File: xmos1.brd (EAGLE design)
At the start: 108 x 69.8 mm, 3 parts

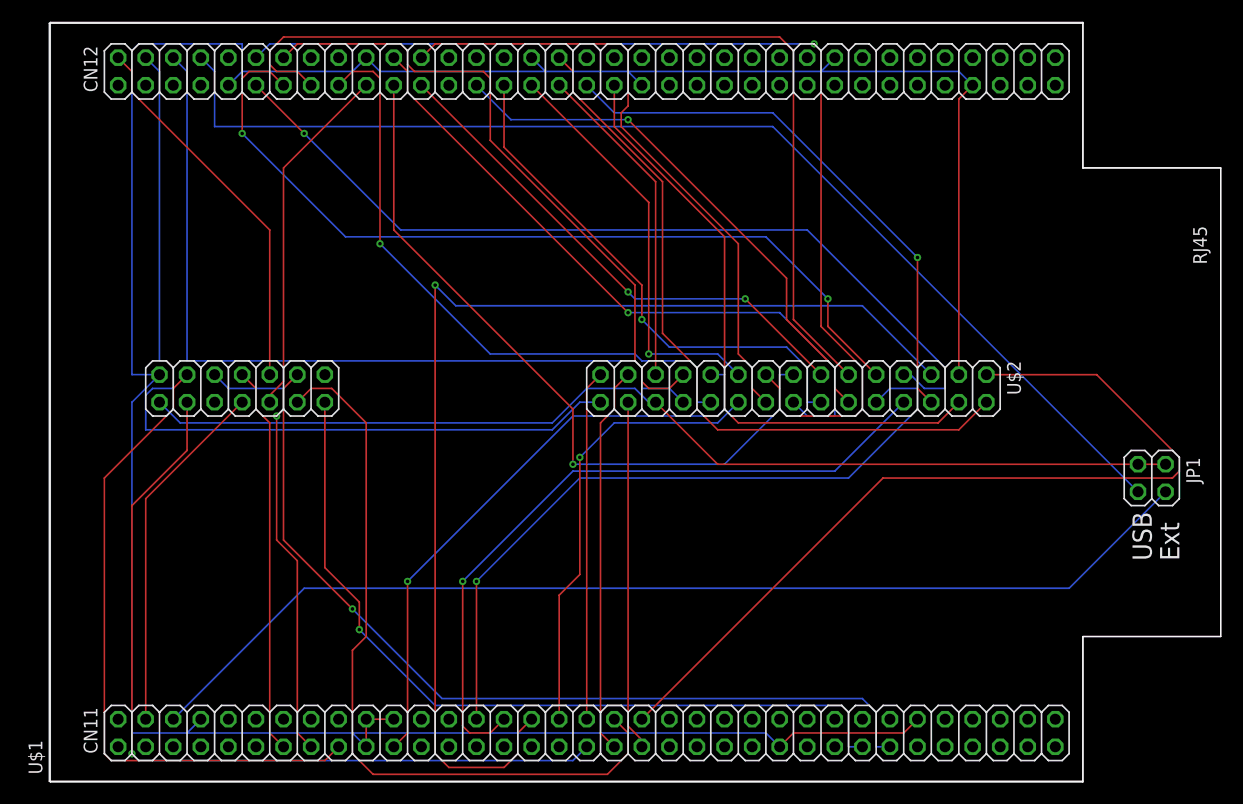
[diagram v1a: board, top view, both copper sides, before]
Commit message: Add the two spare ports to the top. Just needs power now
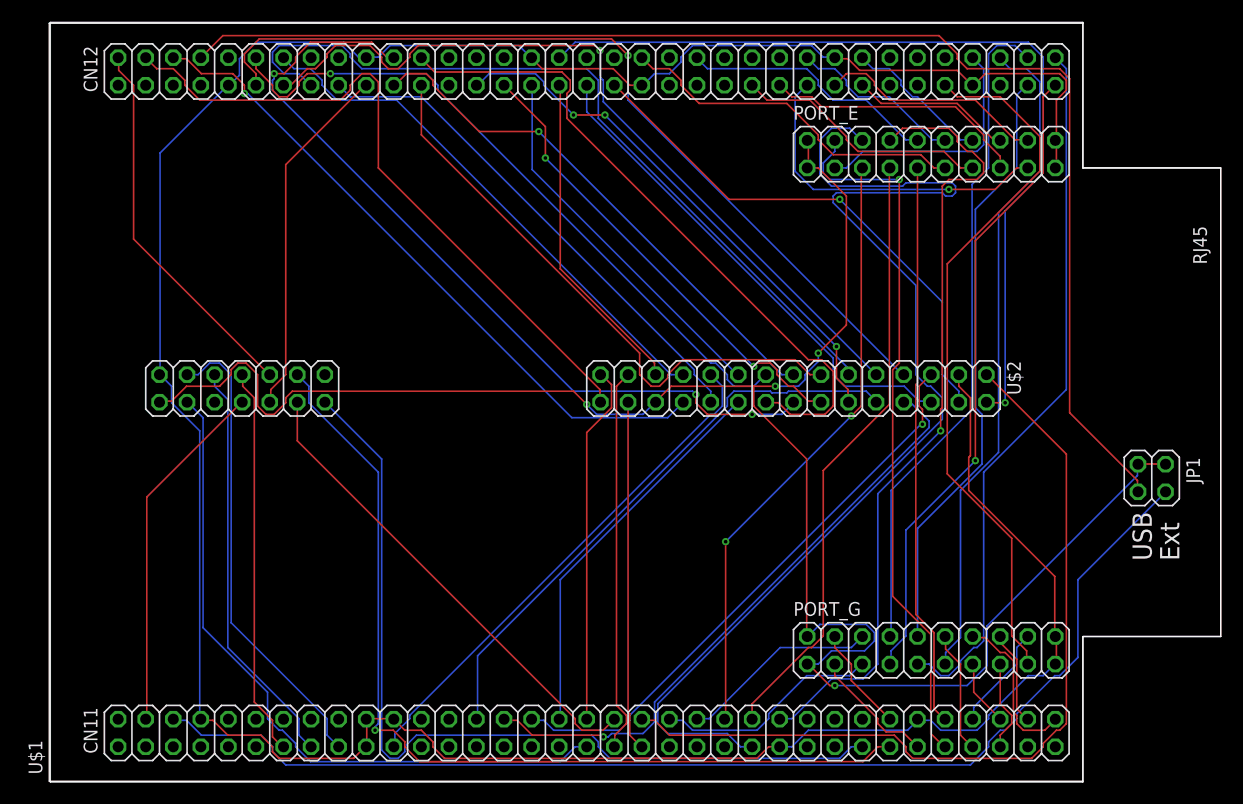
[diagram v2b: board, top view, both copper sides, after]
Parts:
- added PORT_E, PORT_G: (no value), pinhead:2X10
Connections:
- new net N$10: PORT_E.10, U$1.116
- new net N$11: PORT_E.11, U$1.112
- new net N$12: PORT_E.12, U$1.124
- new net N$13: PORT_E.13, U$1.119
- new net N$14: PORT_E.14, U$1.128
- new net N$15: PORT_E.15, U$1.121
- new net N$16: PORT_E.16, U$1.127
- new net N$17: PORT_E.17, U$1.123
- new net N$18: PORT_E.18, U$1.125
- new net N$19: PORT_G.3, U$1.59
- new net N$20: PORT_G.4, U$1.58
- new net N$21: PORT_G.5, U$1.42
- new net N$22: PORT_G.6, U$1.44
- new net N$23: PORT_G.7, U$1.141
- new net N$24: PORT_G.8, U$1.140
- new net N$25: PORT_G.9, U$1.142
- new net N$26: PORT_G.11, U$1.138
- new net N$28: PORT_G.12, U$1.63
- new net N$29: PORT_G.13, U$1.66
- new net N$3: PORT_E.3, U$1.136
- new net N$30: PORT_G.14, U$1.70
- new net N$31: PORT_G.15, U$1.65
- new net N$32: PORT_G.16, U$1.68
- new net N$33: PORT_G.17, U$1.133
- new net N$34: PORT_G.18, U$1.64
- new net N$4: PORT_E.4, U$1.61
- new net N$5: PORT_E.5, U$1.46
- new net N$6: PORT_E.6, U$1.47
- new net N$7: PORT_E.7, U$1.48
- new net N$8: PORT_E.8, U$1.50
- new net N$9: PORT_E.9, U$1.62
- new net PORT_G: PORT_G.10, U$1.139
- net +5V: now also PORT_E.1, PORT_E.2, PORT_G.1, PORT_G.2
- net GND: now also PORT_E.19, PORT_E.20, PORT_G.19, PORT_G.20
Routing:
- net N$6: track 0.00 -> 106.9 mm
- net +5V: track 97.7 -> 179.0 mm, vias 0 -> 4
- net N$8: track 0.00 -> 73.6 mm, vias 0 -> 1
- net N$33: track 0.00 -> 66.0 mm
- net N$25: track 0.00 -> 65.4 mm
- net N$4: track 0.00 -> 65.3 mm, vias 0 -> 1
- net N$26: track 0.00 -> 61.9 mm
- net N$24: track 0.00 -> 61.9 mm
- net N$23: track 0.00 -> 59.7 mm, vias 0 -> 1
- net N$7: track 0.00 -> 56.3 mm
- net N$5: track 0.00 -> 56.1 mm, vias 0 -> 2
- net PORT_G: track 0.00 -> 55.6 mm
- net N$9: track 0.00 -> 52.0 mm
- net A4: track 104.7 -> 53.6 mm
- net A12: track 99.3 -> 63.3 mm
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
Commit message: Add a voltage-regulator option for external power, and clean up the board a bit
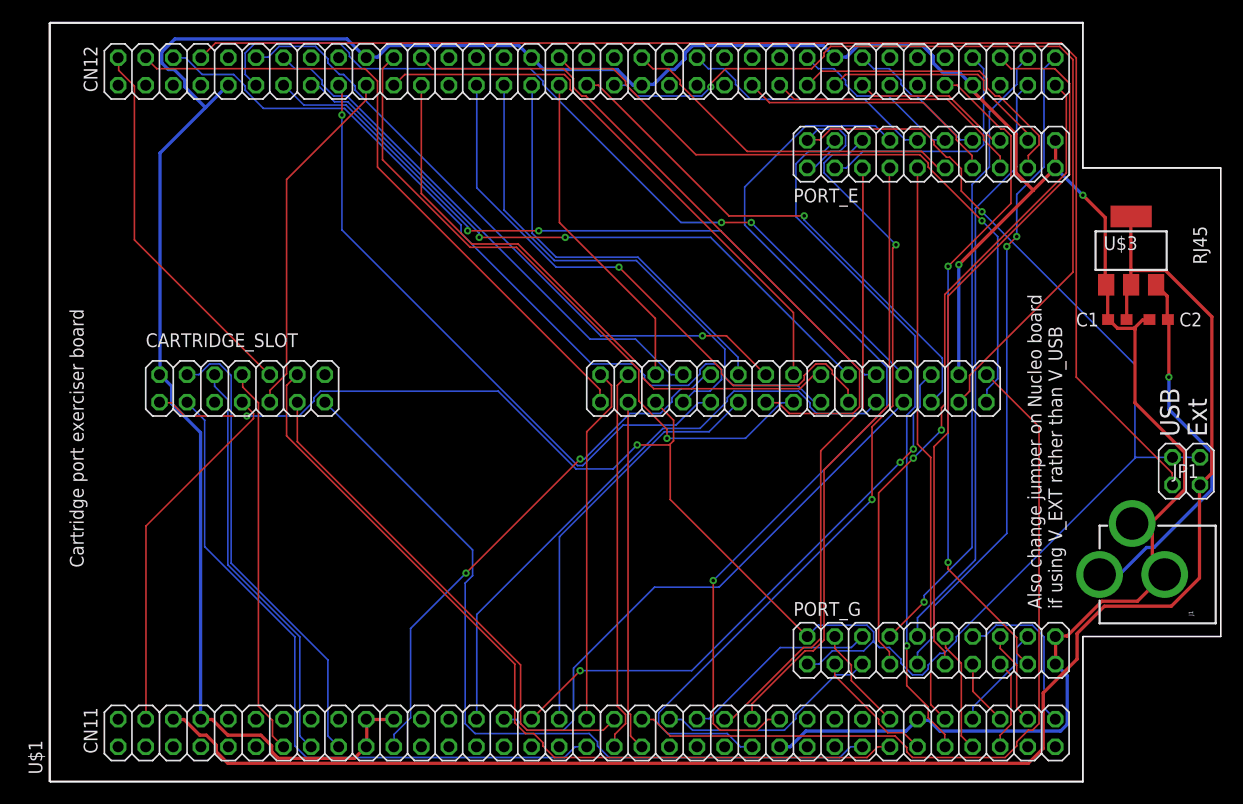
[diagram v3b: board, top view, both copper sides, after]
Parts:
- added C1: 4.7uF, rcl:C0603
- added C2: 1uF, rcl:C0603
- added J1: POWER_JACKPTH, SparkFun-Connectors:POWER_JACK_PTH
- added U$3: LD1117, sjg-power:SOT223
- moved JP1 3.24 mm to (104.8, 29.2)
- renumbered U$2 to CARTRIDGE_SLOT
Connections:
- new net N$27: C2.2, J1.PWR, U$3.3
- net GND: now also C1.1, C2.1, J1.GND, J1.GNDBREAK, U$3.1
- net N$1: now also C1.2, U$3.2, U$3.4
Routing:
- net N$1: track 108.7 -> 151.5 mm
- net N$27: track 0.00 -> 34.6 mm, vias 0 -> 1
- net GND: track 278.4 -> 312.1 mm, vias 0 -> 2
- net A3: track 48.4 -> 81.4 mm
- net N$6: track 106.9 -> 77.4 mm, vias 0 -> 2
- net !BK_SEL_LO!: track 80.8 -> 63.3 mm
- net +5V: track 179.0 -> 194.4 mm, vias 4 -> 3
- net D2: track 76.0 -> 61.9 mm, vias 3 -> 1
- net A7: track 73.8 -> 60.8 mm, vias 0 -> 2
- net D6: track 47.3 -> 58.9 mm, vias 0 -> 1
- net N$8: track 73.6 -> 84.6 mm
- net !BK_SEL_HI!: track 61.8 -> 70.5 mm, vias 1 -> 0
- net A6: track 73.7 -> 65.9 mm, vias 1 -> 2
- net !IRQ!: track 85.5 -> 77.7 mm, vias 1 -> 0
- net !EXTSEL!: track 81.6 -> 74.1 mm
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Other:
- board text added: "Also change jumper on Nucleo board if using V_EXT rather than V_USB"
- board text added: "Cartridge port exerciser board"
